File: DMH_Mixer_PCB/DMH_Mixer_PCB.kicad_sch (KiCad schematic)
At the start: 0 parts

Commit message: PCB work in progress
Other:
- sheet Core Circuit ports: added Clipped Output, Input 1, Input 2, Input 3, Output +, Output -; removed none
- sheet Inputs and Outputs ports: added Input 1 Jack, Input 2 Jack, Input 3 Jack, Output + Jack, Output - Jack, Output Clipped; removed none
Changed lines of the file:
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@@
 		)
 		(instances
-			(project "DMH-Kosmo-5cm-PCB"
+			(project "DMH_Mixer_PCB"
 				(path "/58f4306d-5387-4983-bb08-41a2313fd315"
 					(page "4")
@@
 	)
 	(sheet
-		(at 120.65 80.01)
-		(size 41.91 38.1)
+		(at 49.53 85.09)
+		(size 41.91 33.02)
 		(fields_autoplaced yes)
 		(stroke
@@
 		)
 		(property "Sheetname" "Core Circuit"
-			(at 120.65 79.2984 0)
+			(at 49.53 84.3784 0)
 			(effects
 				(font
@@
 		)
 		(property "Sheetfile" "Core_Circuit.kicad_sch"
-			(at 120.65 118.6946 0)
+			(at 49.53 118.6946 0)
 			(effects
 				(font
@@
 			)
 		)
+		(pin "Input 3" input
+			(at 49.53 96.52 180)
+			(effects
+				(font
+					(size 1.27 1.27)
+				)
+				(justify left)
+			)
+		)
+		(pin "Input 1" input
+			(at 49.53 88.9 180)
+			(effects
+				(font
+					(size 1.27 1.27)
+				)
+				(justify left)
+			)
+		)
+		(pin "Input 2" input
+			(at 49.53 92.71 180)
+			(effects
+				(font
+					(size 1.27 1.27)
+				)
+				(justify left)
+			)
+		)
+		(pin "Clipped Output" input
+			(at 49.53 114.3 180)
+			(effects
+				(font
+					(size 1.27 1.27)
+				)
+				(justify left)
+			)
+		)
+		(pin "Output +" input
+			(at 49.53 110.49 180)
+			(effects
+				(font
+					(size 1.27 1.27)
+				)
+				(justify left)
+			)
+		)
+		(pin "Output -" input
+			(at 49.53 106.68 180)
+			(effects
+				(font
+					(size 1.27 1.27)
+				)
+				(justify left)
+			)
+		)
 		(instances
-			(project "DMH-Kosmo-5cm-PCB"
+			(project "DMH_Mixer_PCB"
 				(path "/58f4306d-5387-4983-bb08-41a2313fd315"
 					(page "3")
@@
 	)
 	(sheet
-		(at 17.78 17.78)
-		(size 20.32 118.11)
+		(at 17.78 76.2)
+		(size 20.32 50.8)
 		(fields_autoplaced yes)
 		(stroke
@@
 		)
 		(property "Sheetname" "Inputs and Outputs"
-			(at 17.78 17.0684 0)
+			(at 17.78 75.4884 0)
 			(effects
 				(font
@@
 		)
 		(property "Sheetfile" "Inputs_and_Outputs.kicad_sch"
-			(at 17.78 136.4746 0)
+			(at 17.78 127.5846 0)
 			(effects
 				(font
@@
 			)
 		)
+		(pin "Input 1 Jack" output
+			(at 38.1 88.9 0)
+			(effects
+				(font
+					(size 1.27 1.27)
+				)
+				(justify right)
+			)
+		)
+		(pin "Input 2 Jack" output
+			(at 38.1 92.71 0)
+			(effects
+				(font
+					(size 1.27 1.27)
+				)
+				(justify right)
+			)
+		)
+		(pin "Input 3 Jack" output
+			(at 38.1 96.52 0)
+			(effects
+				(font
+					(size 1.27 1.27)
+				)
+				(justify right)
+			)
+		)
+		(pin "Output - Jack" input
+			(at 38.1 106.68 0)
+			(effects
+				(font
+					(size 1.27 1.27)
+				)
+				(justify right)
+			)
+		)
+		(pin "Output + Jack" input
+			(at 38.1 110.49 0)
+			(effects
+				(font
+					(size 1.27 1.27)
+				)
+				(justify right)
+			)
+		)
+		(pin "Output Clipped" input
+			(at 38.1 114.3 0)
+			(effects
+				(font
+					(size 1.27 1.27)
+				)
+				(justify right)
+			)
+		)
 		(instances
-			(project "DMH-Kosmo-5cm-PCB"
+			(project "DMH_Mixer_PCB"
 				(path "/58f4306d-5387-4983-bb08-41a2313fd315"
 					(page "2")

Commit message: Component placing in progress
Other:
- sheet Power ports: added none; removed Bus CV, Bus Gate
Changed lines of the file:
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@@
 		(comment 1 "PCB for 5 cm Kosmo format synthesizer module")
 	)
+	(wire
+		(pts
+			(xy 38.1 88.9) (xy 50.8 88.9)
+		)
+		(stroke
+			(width 0)
+			(type default)
+		)
+	)
+	(wire
+		(pts
+			(xy 38.1 114.3) (xy 50.8 114.3)
+		)
+		(stroke
+			(width 0)
+			(type default)
+		)
+	)
+	(wire
+		(pts
+			(xy 38.1 92.71) (xy 50.8 92.71)
+		)
+		(stroke
+			(width 0)
+			(type default)
+		)
+	)
+	(wire
+		(pts
+			(xy 38.1 96.52) (xy 50.8 96.52)
+		)
+		(stroke
+			(width 0)
+			(type default)
+		)
+	)
+	(wire
+		(pts
+			(xy 38.1 110.49) (xy 50.8 110.49)
+		)
+		(stroke
+			(width 0)
+			(type default)
+		)
+	)
+	(wire
+		(pts
+			(xy 38.1 106.68) (xy 50.8 106.68)
+		)
+		(stroke
+			(width 0)
+			(type default)
+		)
+	)
 	(sheet
-		(at 260.35 16.51)
+		(at 101.6 87.63)
 		(size 20.32 27.94)
 		(fields_autoplaced yes)
@@
 		)
 		(property "Sheetname" "Power"
-			(at 260.35 15.7984 0)
+			(at 101.6 86.9184 0)
 			(effects
 				(font
@@
 		)
 		(property "Sheetfile" "Power.kicad_sch"
-			(at 260.35 45.0346 0)
+			(at 101.6 116.1546 0)
 			(effects
 				(font
@@
 				(justify left top)
 				(hide yes)
-			)
-		)
-		(pin "Bus Gate" output
-			(at 260.35 25.4 180)
-			(effects
-				(font
-					(size 1.27 1.27)
-				)
-				(justify left)
-			)
-		)
-		(pin "Bus CV" output
-			(at 260.35 34.29 180)
-			(effects
-				(font
-					(size 1.27 1.27)
-				)
-				(justify left)
 			)
 		)
@@
 	)
 	(sheet
-		(at 49.53 85.09)
-		(size 41.91 33.02)
+		(at 50.8 85.09)
+		(size 38.1 33.02)
 		(fields_autoplaced yes)
 		(stroke
@@
 		)
 		(property "Sheetname" "Core Circuit"
-			(at 49.53 84.3784 0)
+			(at 50.8 84.3784 0)
 			(effects
 				(font
@@
 		)
 		(property "Sheetfile" "Core_Circuit.kicad_sch"
-			(at 49.53 118.6946 0)
+			(at 50.8 118.6946 0)
 			(effects
 				(font
@@
 		)
 		(pin "Input 3" input
-			(at 49.53 96.52 180)
+			(at 50.8 96.52 180)
 			(effects
 				(font
@@
 		)
 		(pin "Input 1" input
-			(at 49.53 88.9 180)
+			(at 50.8 88.9 180)
 			(effects
 				(font
@@
 		)
 		(pin "Input 2" input
-			(at 49.53 92.71 180)
+			(at 50.8 92.71 180)
 			(effects
 				(font
@@
 			)
 		)
-		(pin "Clipped Output" input
-			(at 49.53 114.3 180)
+		(pin "Clipped Output" output
+			(at 50.8 106.68 180)
 			(effects
 				(font
@@
 			)
 		)
-		(pin "Output +" input
-			(at 49.53 110.49 180)
+		(pin "Output -" output
+			(at 50.8 110.49 180)
 			(effects
 				(font
@@
 			)
 		)
-		(pin "Output -" input
-			(at 49.53 106.68 180)
+		(pin "Output +" output
+			(at 50.8 114.3 180)
 			(effects
 				(font

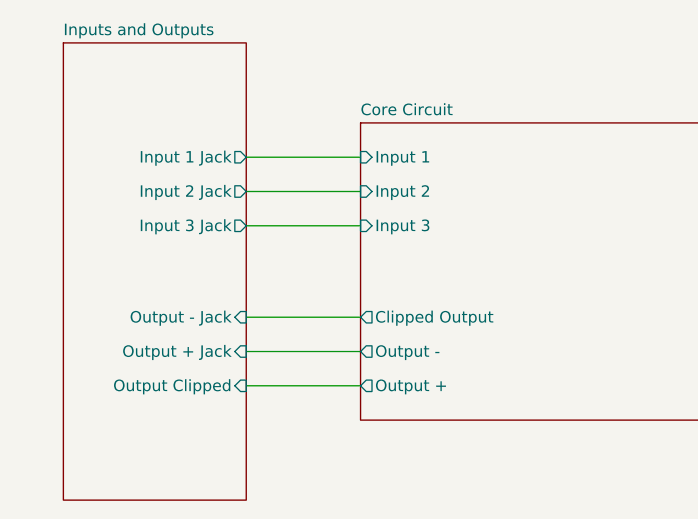
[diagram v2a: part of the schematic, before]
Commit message: Added 4th channel to schematic
... and replaced Inverted Output with Clipped Output
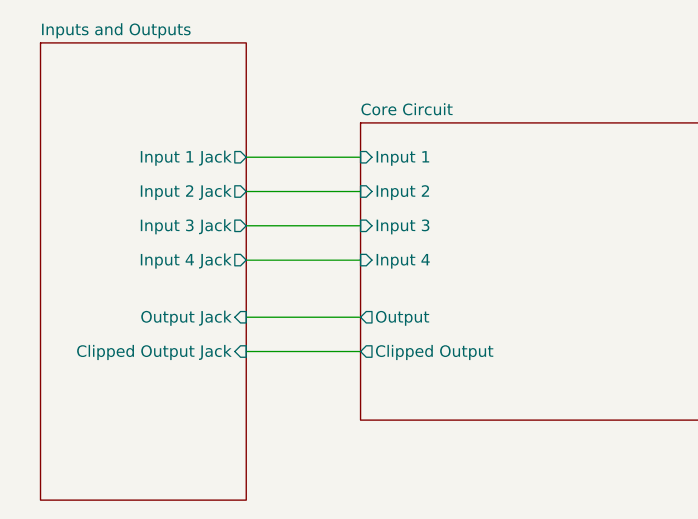
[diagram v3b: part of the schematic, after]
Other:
- sheet Core Circuit ports: added Input 4, Output; removed Output +, Output -
- sheet Inputs and Outputs ports: added Clipped Output Jack, Input 4 Jack, Output Jack; removed Output + Jack, Output - Jack, Output Clipped
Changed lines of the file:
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@@
 	(wire
 		(pts
-			(xy 38.1 114.3) (xy 50.8 114.3)
+			(xy 38.1 110.49) (xy 50.8 110.49)
 		)
 		(stroke
@@
 	(wire
 		(pts
+			(xy 38.1 106.68) (xy 50.8 106.68)
+		)
+		(stroke
+			(width 0)
+			(type default)
+		)
+	)
+	(wire
+		(pts
 			(xy 38.1 96.52) (xy 50.8 96.52)
 		)
@@
 	(wire
 		(pts
-			(xy 38.1 110.49) (xy 50.8 110.49)
-		)
-		(stroke
-			(width 0)
-			(type default)
-		)
-	)
-	(wire
-		(pts
-			(xy 38.1 106.68) (xy 50.8 106.68)
+			(xy 38.1 100.33) (xy 50.8 100.33)
 		)
 		(stroke
@@
 		)
 		(pin "Clipped Output" output
+			(at 50.8 110.49 180)
+			(effects
+				(font
+					(size 1.27 1.27)
+				)
+				(justify left)
+			)
+		)
+		(pin "Output" output
 			(at 50.8 106.68 180)
 			(effects
@@
 			)
 		)
-		(pin "Output -" output
-			(at 50.8 110.49 180)
-			(effects
-				(font
-					(size 1.27 1.27)
-				)
-				(justify left)
-			)
-		)
-		(pin "Output +" output
-			(at 50.8 114.3 180)
+		(pin "Input 4" input
+			(at 50.8 100.33 180)
 			(effects
 				(font
@@
 	)
 	(sheet
-		(at 17.78 76.2)
-		(size 20.32 50.8)
+		(at 15.24 76.2)
+		(size 22.86 50.8)
 		(fields_autoplaced yes)
 		(stroke
@@
 		)
 		(property "Sheetname" "Inputs and Outputs"
-			(at 17.78 75.4884 0)
+			(at 15.24 75.4884 0)
 			(effects
 				(font
@@
 		)
 		(property "Sheetfile" "Inputs_and_Outputs.kicad_sch"
-			(at 17.78 127.5846 0)
+			(at 15.24 127.5846 0)
 			(effects
 				(font
@@
 			)
 		)
-		(pin "Output - Jack" input
+		(pin "Output Jack" input
 			(at 38.1 106.68 0)
 			(effects
@@
 			)
 		)
-		(pin "Output + Jack" input
+		(pin "Clipped Output Jack" input
 			(at 38.1 110.49 0)
 			(effects
@@
 			)
 		)
-		(pin "Output Clipped" input
-			(at 38.1 114.3 0)
-			(effects
-				(font
+		(pin "Input 4 Jack" output
+			(at 38.1 100.33 0)
+			(effects
+				(font

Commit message: Finalization in progress
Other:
- sheet Core Circuit ports: added none; removed Clipped Output
- sheet Inputs and Outputs ports: added none; removed Clipped Output Jack
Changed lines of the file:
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@@
-	(wire
-		(pts
-			(xy 38.1 110.49) (xy 50.8 110.49)
-		)
-		(stroke
-			(width 0)
-			(type default)
-		)
-	)
 	(wire
 		(pts
@@
 			)
 		)
-		(pin "Clipped Output" output
-			(at 50.8 110.49 180)
-			(effects
-				(font
-					(size 1.27 1.27)
-				)
-				(justify left)
-			)
-		)
 		(pin "Output" output
 			(at 50.8 106.68 180)
@@
 			(effects
 				(font
-					(size 1.27 1.27)
-				)
-				(justify right)
-			)
-		)
-		(pin "Clipped Output Jack" input
-			(at 38.1 110.49 0)
-			(effects
-				(font
